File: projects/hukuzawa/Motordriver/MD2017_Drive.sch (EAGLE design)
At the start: 22 parts

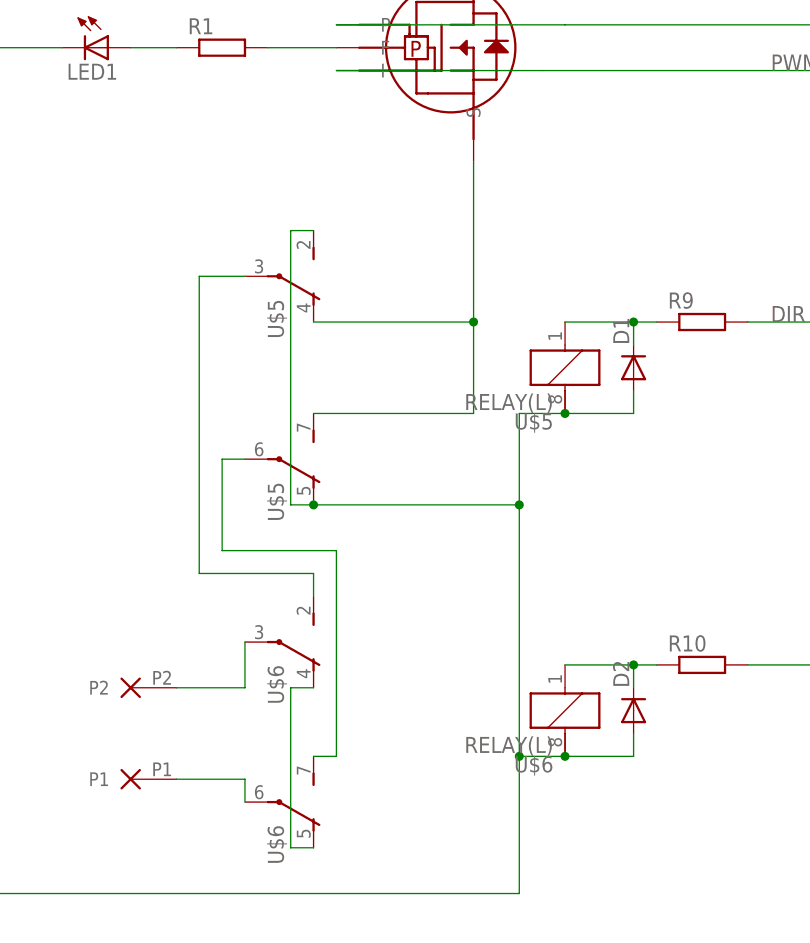
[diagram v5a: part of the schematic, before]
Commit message: モータードライバ駆動部リレー修正
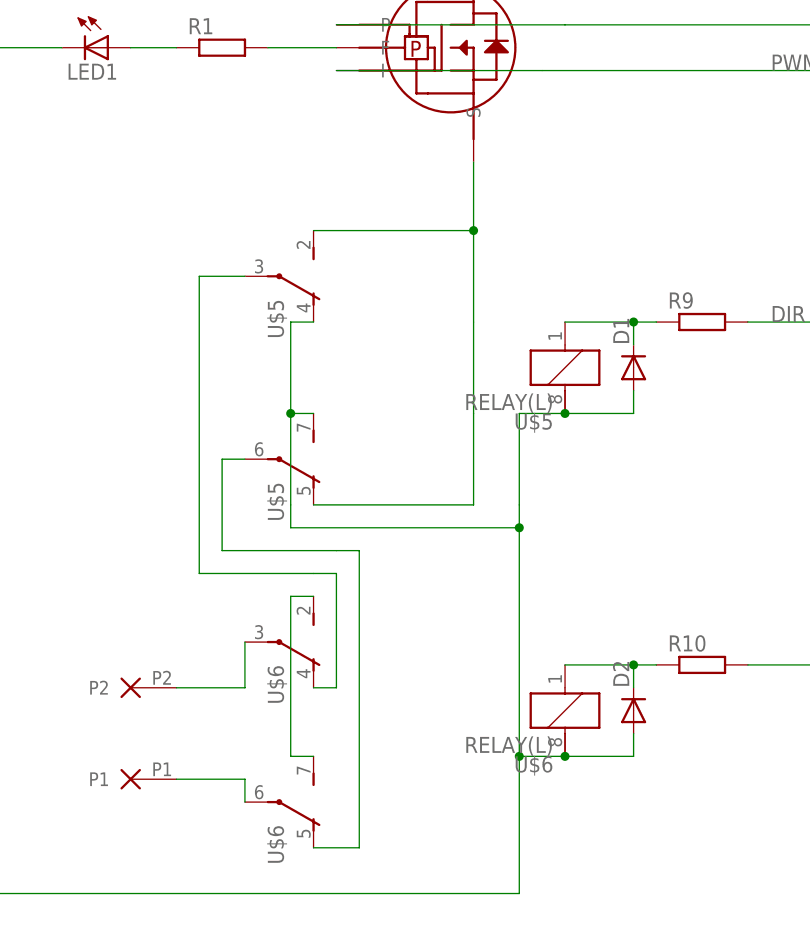
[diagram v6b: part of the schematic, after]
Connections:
- net GND-D: now also U$5R1.S, U$5R2.O; no longer U$5R1.O, U$5R2.S
- net N$1: now also U$6R1.S, U$6R2.S; no longer U$6R1.O, U$6R2.O
- net N$2: now also U$5R1.O, U$5R2.S; no longer U$5R1.S, U$5R2.O
- net N$3: now also U$6R2.O; no longer U$6R2.S
- net N$4: now also U$6R1.O; no longer U$6R1.S
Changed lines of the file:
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@@
 <wire x1="-33.02" y1="-2.54" x2="-33.02" y2="-12.7" width="0.1524" layer="91"/>
 <junction x="-27.94" y="-2.54"/>
-<wire x1="-33.02" y1="-12.7" x2="-33.02" y2="-40.64" width="0.1524" layer="91"/>
+<wire x1="-33.02" y1="-12.7" x2="-33.02" y2="-15.24" width="0.1524" layer="91"/>
+<wire x1="-33.02" y1="-15.24" x2="-33.02" y2="-40.64" width="0.1524" layer="91"/>
 <wire x1="-33.02" y1="-40.64" x2="-33.02" y2="-55.88" width="0.1524" layer="91"/>
 <wire x1="-27.94" y1="-40.64" x2="-33.02" y2="-40.64" width="0.1524" layer="91"/>
 <junction x="-27.94" y="-40.64"/>
 <junction x="-33.02" y="-40.64"/>
-<pinref part="U$5" gate="R2" pin="S"/>
-<wire x1="-55.88" y1="17.78" x2="-58.42" y2="17.78" width="0.1524" layer="91"/>
-<wire x1="-58.42" y1="17.78" x2="-58.42" y2="-12.7" width="0.1524" layer="91"/>
-<pinref part="U$5" gate="R1" pin="O"/>
-<wire x1="-58.42" y1="-12.7" x2="-55.88" y2="-12.7" width="0.1524" layer="91"/>
-<wire x1="-55.88" y1="-12.7" x2="-33.02" y2="-12.7" width="0.1524" layer="91"/>
-<junction x="-55.88" y="-12.7"/>
-<junction x="-33.02" y="-12.7"/>
 <pinref part="LED1" gate="G$1" pin="C"/>
 <wire x1="-83.82" y1="38.1" x2="-93.98" y2="38.1" width="0.1524" layer="91"/>
@@
 <junction x="81.28" y="10.16"/>
 <label x="78.74" y="53.34" size="1.778" layer="95" rot="MR0"/>
+<pinref part="U$5" gate="R2" pin="O"/>
+<wire x1="-58.42" y1="7.62" x2="-58.42" y2="-2.54" width="0.1524" layer="91"/>
+<wire x1="-58.42" y1="-2.54" x2="-58.42" y2="-12.7" width="0.1524" layer="91"/>
+<wire x1="-55.88" y1="7.62" x2="-58.42" y2="7.62" width="0.1524" layer="91"/>
+<pinref part="U$5" gate="R1" pin="S"/>
+<wire x1="-55.88" y1="-2.54" x2="-58.42" y2="-2.54" width="0.1524" layer="91"/>
+<junction x="-58.42" y="-2.54"/>
+<wire x1="-33.02" y1="-15.24" x2="-58.42" y2="-15.24" width="0.1524" layer="91"/>
+<wire x1="-58.42" y1="-15.24" x2="-58.42" y2="-12.7" width="0.1524" layer="91"/>
+<junction x="-33.02" y="-15.24"/>
 </segment>
 </net>
@@
 <segment>
 <pinref part="U$4" gate="G$1" pin="S"/>
-<wire x1="-38.1" y1="25.4" x2="-38.1" y2="7.62" width="0.1524" layer="91"/>
-<pinref part="U$5" gate="R2" pin="O"/>
-<wire x1="-38.1" y1="7.62" x2="-55.88" y2="7.62" width="0.1524" layer="91"/>
-<pinref part="U$5" gate="R1" pin="S"/>
-<wire x1="-55.88" y1="-2.54" x2="-38.1" y2="-2.54" width="0.1524" layer="91"/>
+<wire x1="-38.1" y1="25.4" x2="-38.1" y2="17.78" width="0.1524" layer="91"/>
+<wire x1="-38.1" y1="17.78" x2="-38.1" y2="7.62" width="0.1524" layer="91"/>
 <wire x1="-38.1" y1="-2.54" x2="-38.1" y2="7.62" width="0.1524" layer="91"/>
-<junction x="-38.1" y="7.62"/>
+<pinref part="U$5" gate="R1" pin="O"/>
+<wire x1="-55.88" y1="-12.7" x2="-38.1" y2="-12.7" width="0.1524" layer="91"/>
+<wire x1="-38.1" y1="-12.7" x2="-38.1" y2="-2.54" width="0.1524" layer="91"/>
+<pinref part="U$5" gate="R2" pin="S"/>
+<wire x1="-55.88" y1="17.78" x2="-38.1" y2="17.78" width="0.1524" layer="91"/>
+<junction x="-38.1" y="17.78"/>
 </segment>
 </net>
@@
 <pinref part="U$5" gate="R2" pin="P"/>
 <wire x1="-68.58" y1="12.7" x2="-63.5" y2="12.7" width="0.1524" layer="91"/>
-<pinref part="U$6" gate="R2" pin="S"/>
-<wire x1="-55.88" y1="-22.86" x2="-55.88" y2="-20.32" width="0.1524" layer="91"/>
+<wire x1="-55.88" y1="-20.32" x2="-53.34" y2="-20.32" width="0.1524" layer="91"/>
+<wire x1="-53.34" y1="-20.32" x2="-53.34" y2="-33.02" width="0.1524" layer="91"/>
+<pinref part="U$6" gate="R2" pin="O"/>
+<wire x1="-53.34" y1="-33.02" x2="-55.88" y2="-33.02" width="0.1524" layer="91"/>
 </segment>
 </net>
@@
 <pinref part="U$5" gate="R1" pin="P"/>
 <wire x1="-66.04" y1="-7.62" x2="-63.5" y2="-7.62" width="0.1524" layer="91"/>
-<pinref part="U$6" gate="R1" pin="S"/>
-<wire x1="-55.88" y1="-40.64" x2="-53.34" y2="-40.64" width="0.1524" layer="91"/>
-<wire x1="-53.34" y1="-40.64" x2="-53.34" y2="-17.78" width="0.1524" layer="91"/>
 <wire x1="-53.34" y1="-17.78" x2="-66.04" y2="-17.78" width="0.1524" layer="91"/>
-</segment>
-</net>
-<net name="N$1" class="0">
-<segment>
-<pinref part="U$6" gate="R2" pin="O"/>
-<wire x1="-55.88" y1="-33.02" x2="-58.42" y2="-33.02" width="0.1524" layer="91"/>
-<wire x1="-58.42" y1="-33.02" x2="-58.42" y2="-50.8" width="0.1524" layer="91"/>
+<wire x1="-53.34" y1="-17.78" x2="-50.8" y2="-17.78" width="0.1524" layer="91"/>
+<wire x1="-50.8" y1="-17.78" x2="-50.8" y2="-50.8" width="0.1524" layer="91"/>
 <pinref part="U$6" gate="R1" pin="O"/>
-<wire x1="-58.42" y1="-50.8" x2="-55.88" y2="-50.8" width="0.1524" layer="91"/>
+<wire x1="-50.8" y1="-50.8" x2="-55.88" y2="-50.8" width="0.1524" layer="91"/>
 </segment>
 </net>
@@
 </segment>
 </net>
+<net name="N$1" class="0">
+<segment>
+<pinref part="U$6" gate="R2" pin="S"/>
+<wire x1="-55.88" y1="-22.86" x2="-58.42" y2="-22.86" width="0.1524" layer="91"/>
+<wire x1="-58.42" y1="-22.86" x2="-58.42" y2="-40.64" width="0.1524" layer="91"/>
+<pinref part="U$6" gate="R1" pin="S"/>
+<wire x1="-58.42" y1="-40.64" x2="-55.88" y2="-40.64" width="0.1524" layer="91"/>
+</segment>
+</net>

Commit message: モータードライバ全ボード図修正
配置の基準単位をmilに変更して再配置・再配線
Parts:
- R2, R3, R4, R5, R6, R7, R8: value (none) -> 300
- renumbered U$4 to FET1
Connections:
- net N$1 renamed BRAKES
- net N$10 renamed PROTECTSP.
- net N$2 renamed PWMOUT
- net N$3 renamed DIRP
- net N$4 renamed DIRN
- net N$5 renamed OUTN
- net N$6 renamed OUTP
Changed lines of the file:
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@@
 <part name="POWERPPORT" library="FH105" deviceset="8PIN" device=""/>
 <part name="POWERNPORT" library="FH105" deviceset="8PIN" device=""/>
-<part name="U$4" library="BUK116-50L" deviceset="BUK116-50L" device=""/>
+<part name="FET1" library="BUK116-50L" deviceset="BUK116-50L" device=""/>
 <part name="U$5" library="relay" deviceset="RELAY(L)" device=""/>
 <part name="U$6" library="relay" deviceset="RELAY(L)" device=""/>
@@
 <part name="LED1" library="FP-21T for MITS" deviceset="LED" device="5MM"/>
 <part name="R1" library="rcl" deviceset="R-EU_" device="R3216W"/>
-<part name="R2" library="rcl" deviceset="R-EU_" device="R3216W"/>
-<part name="R3" library="rcl" deviceset="R-EU_" device="R3216W"/>
-<part name="R4" library="rcl" deviceset="R-EU_" device="R3216W"/>
-<part name="R5" library="rcl" deviceset="R-EU_" device="R3216W"/>
-<part name="R6" library="rcl" deviceset="R-EU_" device="R3216W"/>
-<part name="R7" library="rcl" deviceset="R-EU_" device="R3216W"/>
-<part name="R8" library="rcl" deviceset="R-EU_" device="R3216W"/>
+<part name="R2" library="rcl" deviceset="R-EU_" device="R3216W" value="300"/>
+<part name="R3" library="rcl" deviceset="R-EU_" device="R3216W" value="300"/>
+<part name="R4" library="rcl" deviceset="R-EU_" device="R3216W" value="300"/>
+<part name="R5" library="rcl" deviceset="R-EU_" device="R3216W" value="300"/>
+<part name="R6" library="rcl" deviceset="R-EU_" device="R3216W" value="300"/>
+<part name="R7" library="rcl" deviceset="R-EU_" device="R3216W" value="300"/>
+<part name="R8" library="rcl" deviceset="R-EU_" device="R3216W" value="300"/>
 <part name="U$9" library="Powerio" deviceset="2P" device=""/>
 <part name="R9" library="rcl" deviceset="R-EU_" device="R3216W"/>
@@
 <instance part="POWERNPORT" gate="-7" x="86.36" y="10.16"/>
 <instance part="POWERNPORT" gate="-1" x="86.36" y="40.64"/>
-<instance part="U$4" gate="G$1" x="-40.64" y="38.1"/>
+<instance part="FET1" gate="G$1" x="-40.64" y="38.1"/>
 <instance part="U$5" gate="R1" x="-58.42" y="-7.62" rot="R270"/>
 <instance part="U$5" gate="1" x="-27.94" y="2.54" rot="R180"/>
@@
 </segment>
 </net>
-<net name="N$10" class="0">
+<net name="PROTECTSP." class="0">
 <segment>
 <pinref part="U$8" gate="A" pin="EMIT"/>
@@
 <wire x1="7.62" y1="22.86" x2="5.08" y2="22.86" width="0.1524" layer="91"/>
 <junction x="7.62" y="22.86"/>
-<pinref part="U$4" gate="G$1" pin="P"/>
+<pinref part="FET1" gate="G$1" pin="P"/>
 <wire x1="-27.94" y1="40.64" x2="-53.34" y2="40.64" width="0.1524" layer="91"/>
 <wire x1="-27.94" y1="40.64" x2="5.08" y2="40.64" width="0.1524" layer="91"/>
 <wire x1="5.08" y1="40.64" x2="5.08" y2="22.86" width="0.1524" layer="91"/>
 <junction x="5.08" y="22.86"/>
+<label x="5.08" y="40.64" size="1.778" layer="95" rot="MR0"/>
 </segment>
 </net>
@@
 <segment>
 <wire x1="2.54" y1="2.54" x2="2.54" y2="20.32" width="0.1524" layer="91"/>
-<pinref part="U$4" gate="G$1" pin="I"/>
+<pinref part="FET1" gate="G$1" pin="I"/>
 <wire x1="-30.48" y1="35.56" x2="-53.34" y2="35.56" width="0.1524" layer="91"/>
 <label x="-5.08" y="35.56" size="1.778" layer="95"/>
@@
 </segment>
 </net>
-<net name="N$2" class="0">
-<segment>
-<pinref part="U$4" gate="G$1" pin="S"/>
+<net name="PWMOUT" class="0">
+<segment>
+<pinref part="FET1" gate="G$1" pin="S"/>
 <wire x1="-38.1" y1="25.4" x2="-38.1" y2="17.78" width="0.1524" layer="91"/>
 <wire x1="-38.1" y1="17.78" x2="-38.1" y2="7.62" width="0.1524" layer="91"/>
@@
 </segment>
 </net>
-<net name="N$3" class="0">
+<net name="DIRP" class="0">
 <segment>
 <wire x1="-55.88" y1="-20.32" x2="-68.58" y2="-20.32" width="0.1524" layer="91"/>
@@
 </segment>
 </net>
-<net name="N$4" class="0">
+<net name="DIRN" class="0">
 <segment>
 <wire x1="-66.04" y1="-17.78" x2="-66.04" y2="-7.62" width="0.1524" layer="91"/>
@@
 </segment>
 </net>
-<net name="N$5" class="0">
+<net name="OUTN" class="0">
 <segment>
 <pinref part="U$9" gate="G1" pin="P1"/>
@@
 </segment>
 </net>
-<net name="N$6" class="0">
+<net name="OUTP" class="0">
 <segment>
 <pinref part="U$9" gate="G1" pin="P2"/>
@@
 <segment>
 <pinref part="R1" gate="G$1" pin="2"/>
-<pinref part="U$4" gate="G$1" pin="F"/>
+<pinref part="FET1" gate="G$1" pin="F"/>
 <wire x1="-60.96" y1="38.1" x2="-53.34" y2="38.1" width="0.1524" layer="91"/>
 </segment>
@@
 <net name="VCC12V" class="0">
 <segment>
-<pinref part="U$4" gate="G$1" pin="D"/>
+<pinref part="FET1" gate="G$1" pin="D"/>
 <pinref part="POWERPPORT" gate="-1" pin="P$1"/>
 <wire x1="-38.1" y1="50.8" x2="12.7" y2="50.8" width="0.1524" layer="91"/>
@@
 </segment>
 </net>
-<net name="N$1" class="0">
+<net name="BRAKES" class="0">
 <segment>
 <pinref part="U$6" gate="R2" pin="S"/>
